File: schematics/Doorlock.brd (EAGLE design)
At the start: 65 x 56 mm, 40 parts, among them IC1 AT90S2313S, J1 RJ45, K1 G5V1, K2 G5V1, X1 RASPI_BOARD_B+#_H, X2 RIA182-04, X4 RIA182-05

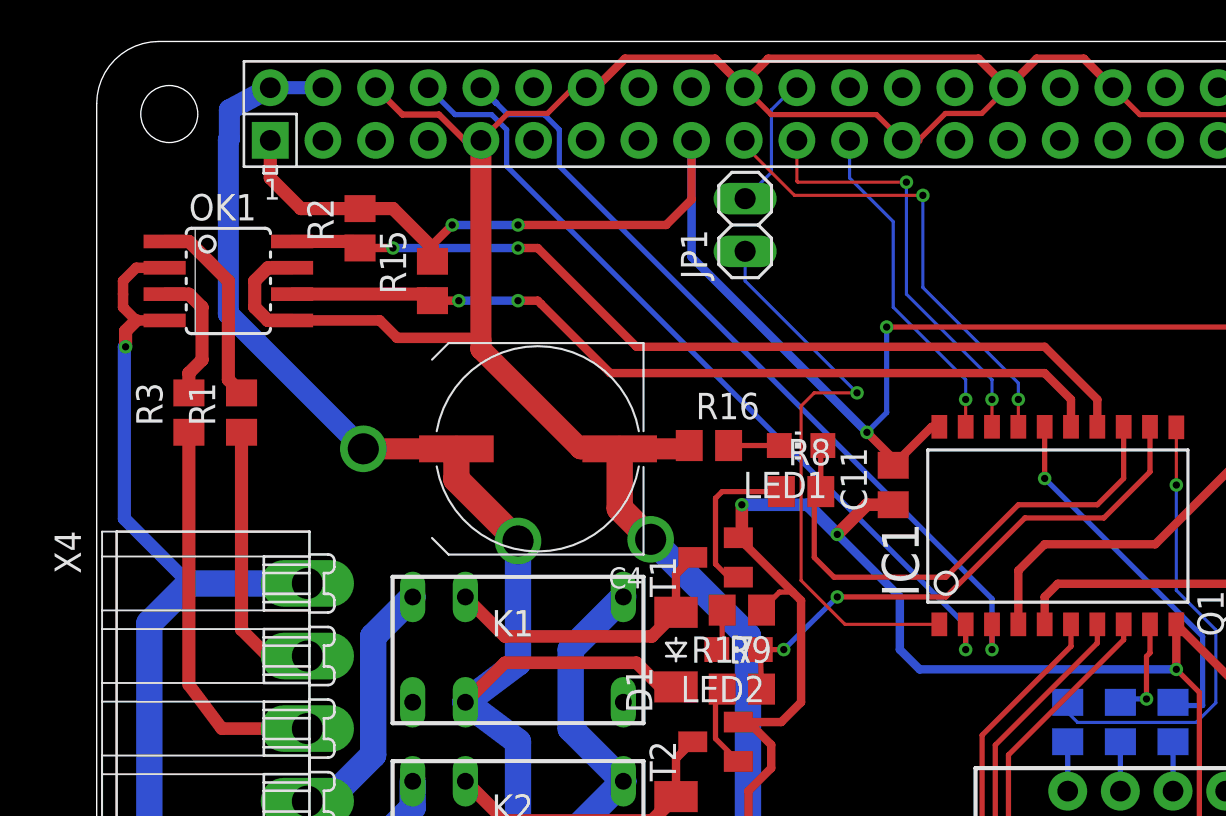
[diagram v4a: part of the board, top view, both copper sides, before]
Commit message: schematics: decouple optocoupler
Signed-off-by: Ralf Ramsauer <ralf@binary-kitchen.de>
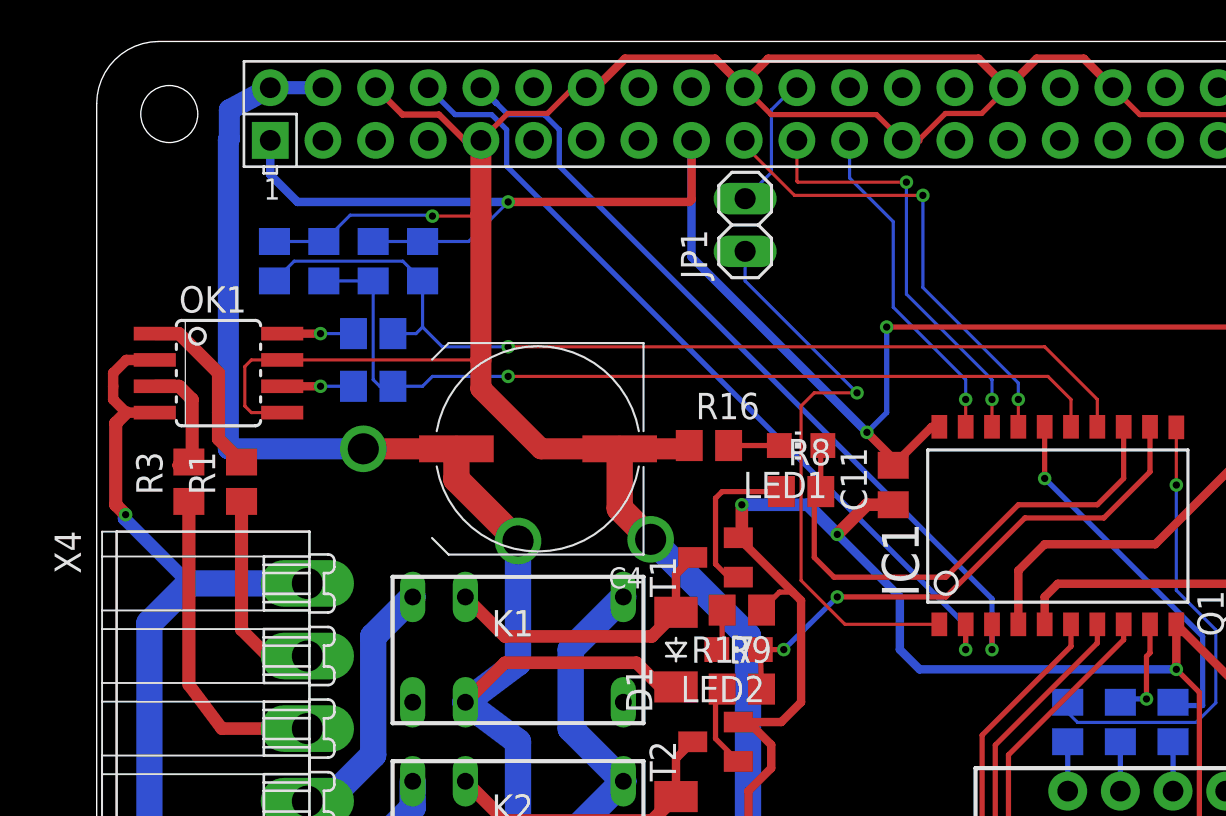
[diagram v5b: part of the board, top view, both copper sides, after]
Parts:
- added C5, C6: 100n, rcl:C0805
- added R18, R19: 1k, rcl:R0805
- R15, R2: value 1k -> 10k
- moved OK1 4.47 mm to (5.87, 40.0)
- moved R2 3.41 mm to (15.7, 45.4), flipped to the bottom
- moved R1 3.33 mm to (6.99, 34.8)
- moved R3 3.33 mm to (4.45, 34.8)
- moved R15 3.01 mm to (13.3, 45.4), flipped to the bottom
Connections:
- new net N$3: OK1.6, R18.1
- new net N$5: OK1.8, R19.1
- net EMERGENCY_UNLOCK: now also C6.1, R18.2; no longer OK1.6
- net GND: now also C5.2, C6.2
- net TUERSTATUS: now also C5.1, R19.2; no longer OK1.8
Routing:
- net GND: track 264.3 -> 276.4 mm, vias 5 -> 6
- net VCC: track 110.3 -> 115.0 mm, vias 4 -> 3
- net GND2: track 68.0 -> 63.7 mm
- net +5V: track 82.9 -> 86.7 mm
- net TUERSTATUS: track 43.3 -> 47.0 mm, vias 2 -> 1
- net N$5: track 0.00 -> 3.44 mm, vias 0 -> 1
- net N$3: track 0.00 -> 3.44 mm, vias 0 -> 1
- net N$13: track 18.9 -> 15.6 mm
- net N$10: track 13.2 -> 9.89 mm
- net EMERGENCY_UNLOCK: track 41.0 -> 42.9 mm, vias 2 -> 1
- net N$14: track 9.53 -> 8.61 mm

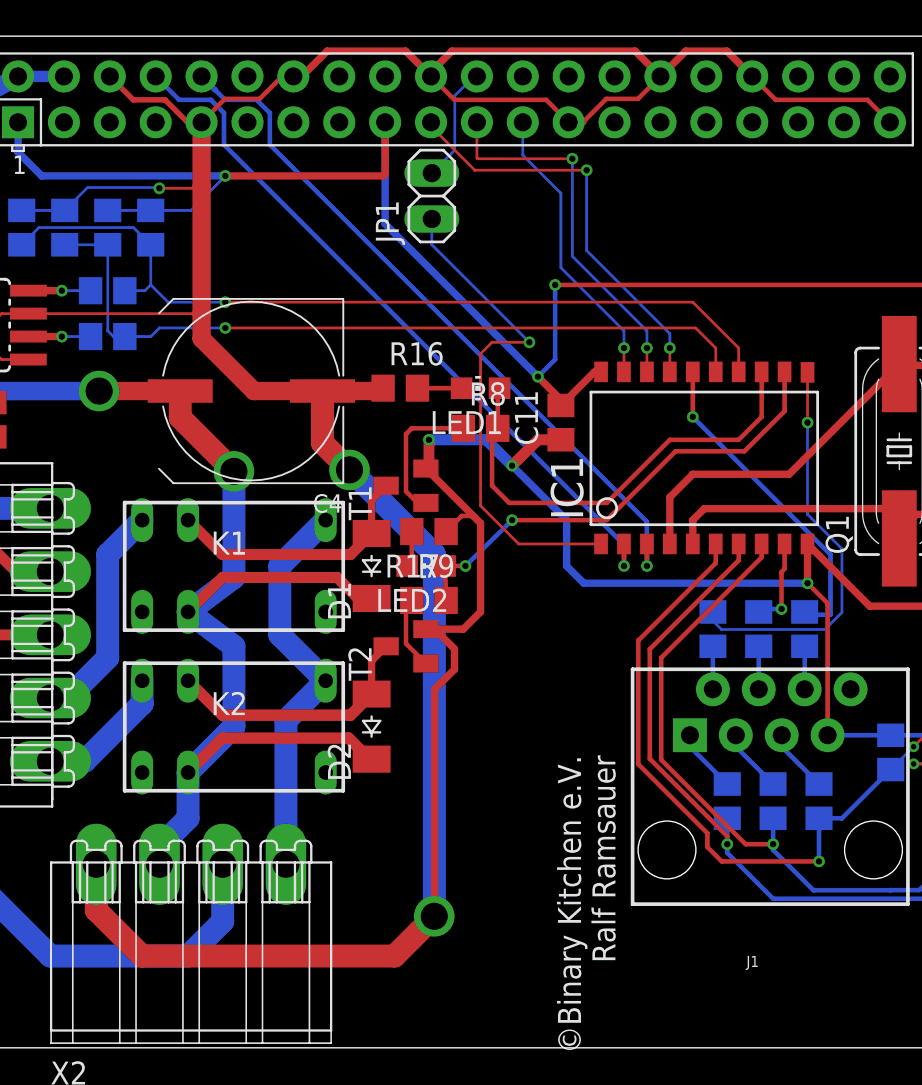
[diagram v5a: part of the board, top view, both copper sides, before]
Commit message: schematics: board: rearrange LEDs
Signed-off-by: Ralf Ramsauer <ralf@binary-kitchen.de>
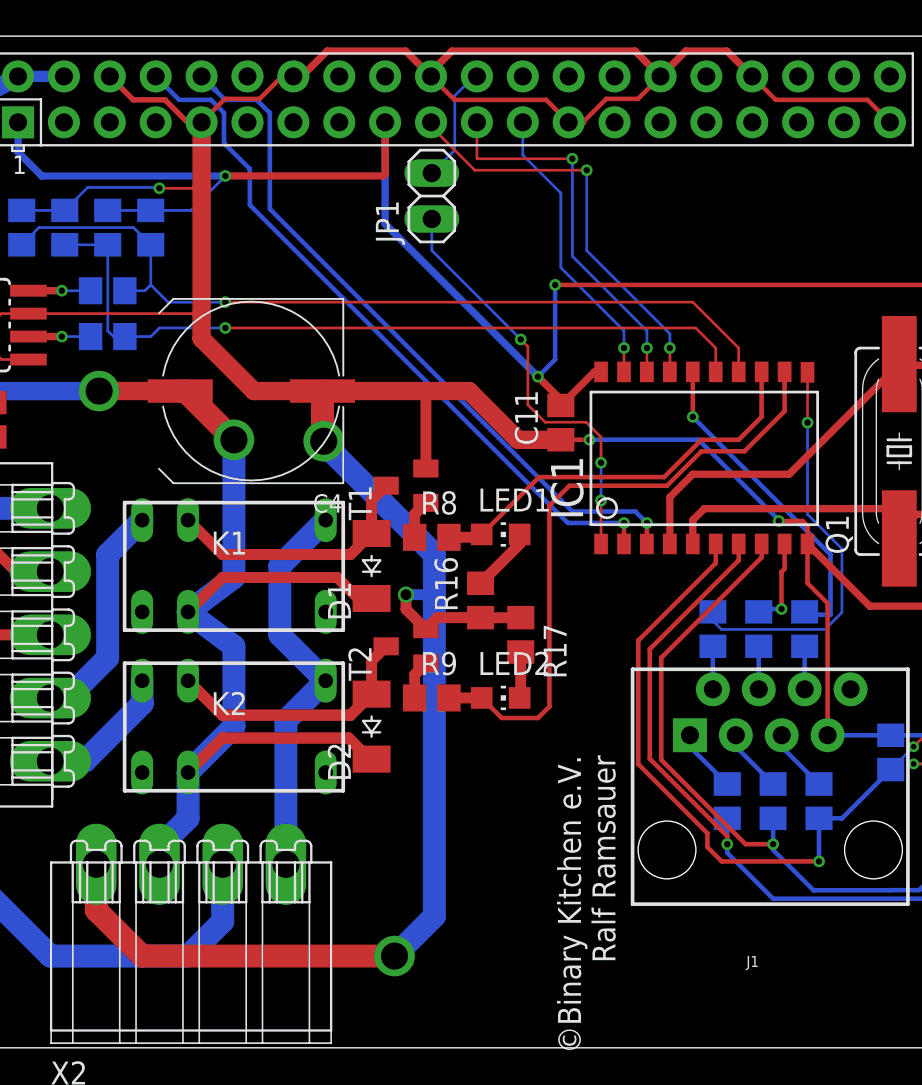
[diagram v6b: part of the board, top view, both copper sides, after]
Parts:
- moved R16 12.6 mm to (34.0, 24.8), turned to 90 degrees
- moved LED2 8.39 mm to (35.1, 19.4), turned to 270 degrees
- moved LED1 8.17 mm to (35.1, 28.4), turned to 270 degrees
- moved R17 7.65 mm to (36.2, 22.9), turned to 270 degrees
- moved R8 6.61 mm to (31.3, 28.3)
- moved R9 5.40 mm to (31.3, 19.4)
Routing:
- net GND: track 276.4 -> 255.2 mm
- net SCHNAPPER: track 26.4 -> 34.8 mm, vias 2 -> 0
- net N$27: track 7.85 -> 2.16 mm
- net N$1: track 28.0 -> 23.2 mm, vias 1 -> 3
- net BOLZEN: track 25.3 -> 22.8 mm
- net N$28: track 4.08 -> 2.16 mm
- net N$16: track 2.45 -> 3.60 mm
- net RXD: track 40.1 -> 39.5 mm
- net N$17: track 2.01 -> 2.57 mm

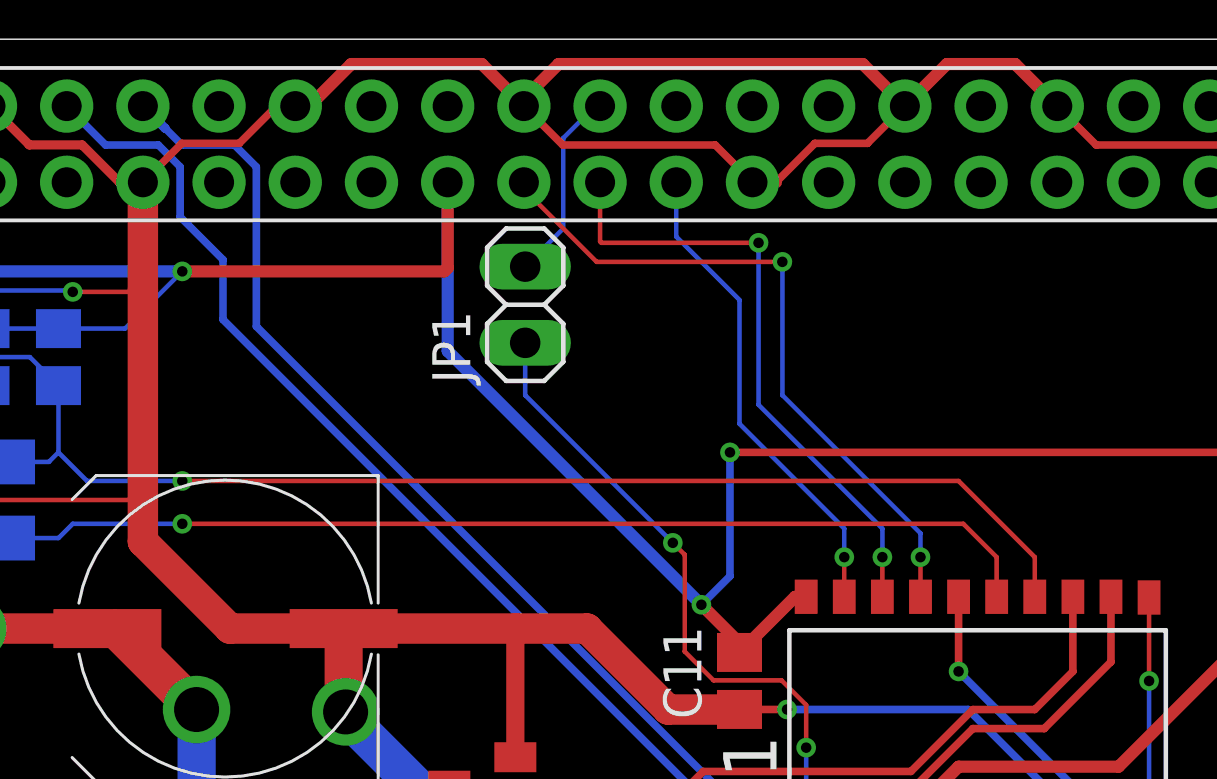
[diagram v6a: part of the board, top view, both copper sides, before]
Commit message: schematics: add door state jumper
Signed-off-by: Ralf Ramsauer <ralf@binary-kitchen.de>
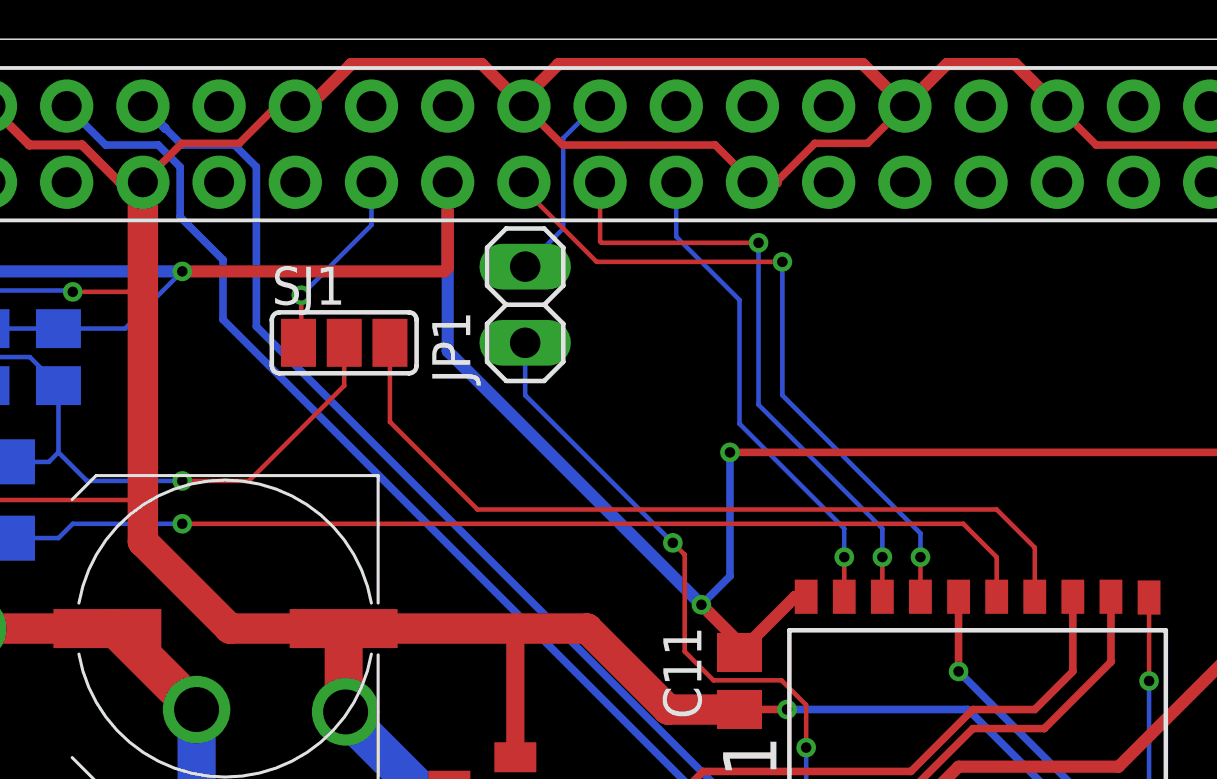
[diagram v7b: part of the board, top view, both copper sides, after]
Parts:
- added SJ1: (no value), jumper:SJ_2
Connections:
- new net TUERSTATUS_AVR: IC1.14, SJ1.3
- new net TUERSTATUS_PI: SJ1.1, X1.15
- net TUERSTATUS: now also SJ1.2; no longer IC1.14
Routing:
- net TUERSTATUS_AVR: track 0.00 -> 27.5 mm
- net TUERSTATUS: track 47.0 -> 24.4 mm
- net TUERSTATUS_PI: track 0.00 -> 6.36 mm, vias 0 -> 1
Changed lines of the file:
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@@
 <element name="R18" library="rcl" package="R0805" value="1k" x="13.335" y="39.37" rot="MR180"/>
 <element name="R19" library="rcl" package="R0805" value="1k" x="13.335" y="41.91" rot="MR180"/>
+<element name="SJ1" library="jumper" library_urn="urn:adsk.eagle:library:252" package="SJ_2" package3d_urn="urn:adsk.eagle:package:15474/1" value="" x="25.24125" y="45.87875"/>
 </elements>
 <signals>
@@
 <signal name="TUERSTATUS">
 <contactref element="R2" pad="1"/>
-<contactref element="IC1" pad="14"/>
 <via x="19.84375" y="41.275" extent="1-16" drill="0.35"/>
-<wire x1="45.72" y1="41.275" x2="48.26" y2="38.735" width="0.1524" layer="1"/>
-<wire x1="48.26" y1="38.735" x2="48.26" y2="37.4142" width="0.1524" layer="1"/>
-<wire x1="19.84375" y1="41.275" x2="45.72" y2="41.275" width="0.1524" layer="1"/>
 <contactref element="R19" pad="2"/>
 <contactref element="C5" pad="1"/>
@@
 <wire x1="15.71625" y1="42.2275" x2="16.66875" y2="41.275" width="0.1524" layer="16"/>
 <wire x1="16.66875" y1="41.275" x2="19.84375" y2="41.275" width="0.1524" layer="16"/>
+<contactref element="SJ1" pad="2"/>
+<wire x1="19.84375" y1="41.275" x2="22.06625" y2="41.275" width="0.1524" layer="1"/>
+<wire x1="22.06625" y1="41.275" x2="25.24125" y2="44.45" width="0.1524" layer="1"/>
+<wire x1="25.24125" y1="44.45" x2="25.24125" y2="45.87875" width="0.1524" layer="1"/>
 </signal>
 <signal name="N$10">
@@
 <wire x1="10.795" y1="41.91" x2="12.385" y2="41.91" width="0.1524" layer="16"/>
 </signal>
+<signal name="TUERSTATUS_AVR">
+<contactref element="SJ1" pad="3"/>
+<contactref element="IC1" pad="14"/>
+<wire x1="26.76525" y1="45.87875" x2="26.76525" y2="43.2435" width="0.1524" layer="1"/>
+<wire x1="26.76525" y1="43.2435" x2="29.68625" y2="40.3225" width="0.1524" layer="1"/>
+<wire x1="29.68625" y1="40.3225" x2="46.99" y2="40.3225" width="0.1524" layer="1"/>
+<wire x1="46.99" y1="40.3225" x2="48.26" y2="39.0525" width="0.1524" layer="1"/>
+<wire x1="48.26" y1="39.0525" x2="48.26" y2="37.4142" width="0.1524" layer="1"/>
+</signal>
+<signal name="TUERSTATUS_PI">
+<contactref element="SJ1" pad="1"/>
+<contactref element="X1" pad="15"/>
+<wire x1="23.71725" y1="45.87875" x2="23.8125" y2="45.974" width="0.1524" layer="1"/>
+<wire x1="23.8125" y1="45.974" x2="23.8125" y2="47.46625" width="0.1524" layer="1"/>
+<via x="23.8125" y="47.46625" extent="1-16" drill="0.35"/>
+<wire x1="23.8125" y1="47.46625" x2="26.15" y2="49.80375" width="0.1524" layer="16"/>
+<wire x1="26.15" y1="49.80375" x2="26.15" y2="51.23" width="0.1524" layer="16"/>
+</signal>
 </signals>

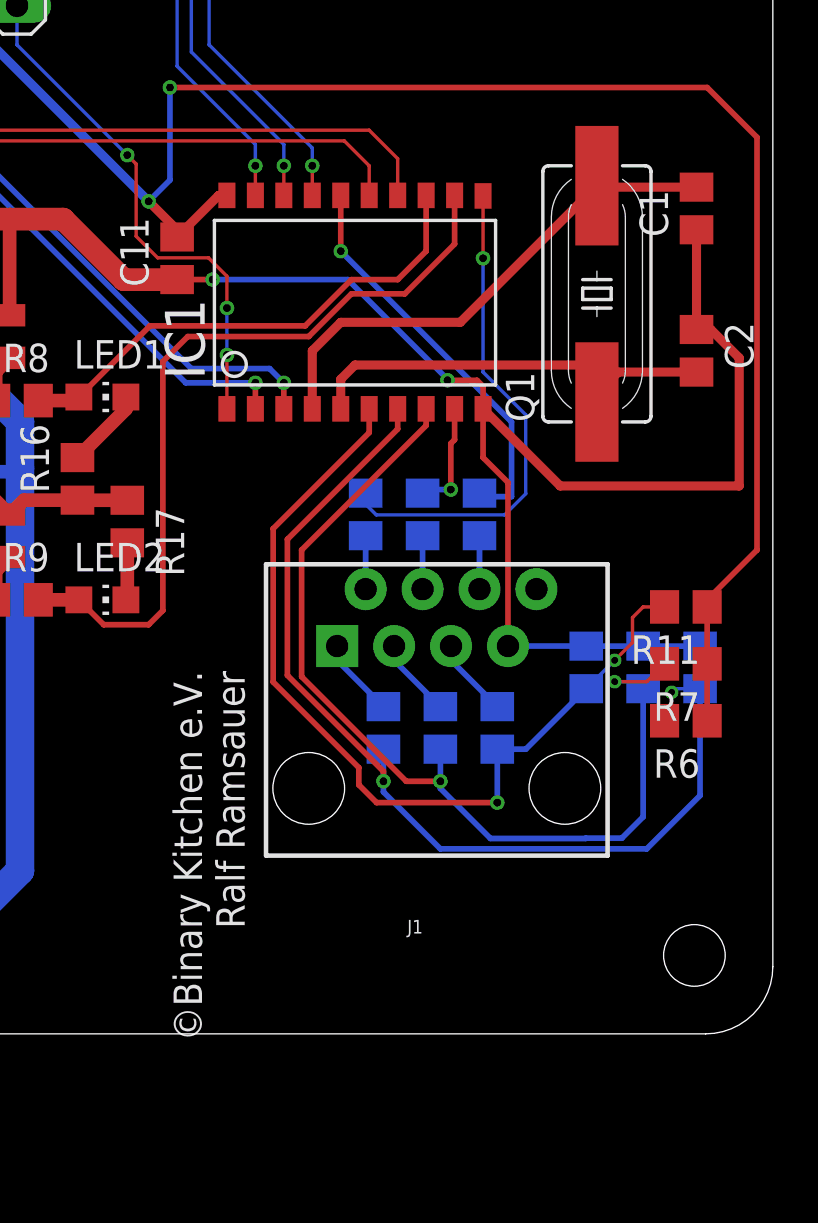
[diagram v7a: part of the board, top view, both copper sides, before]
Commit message: schematics: board: move RJ45 jack to the left
Signed-off-by: Ralf Ramsauer <ralf@binary-kitchen.de>
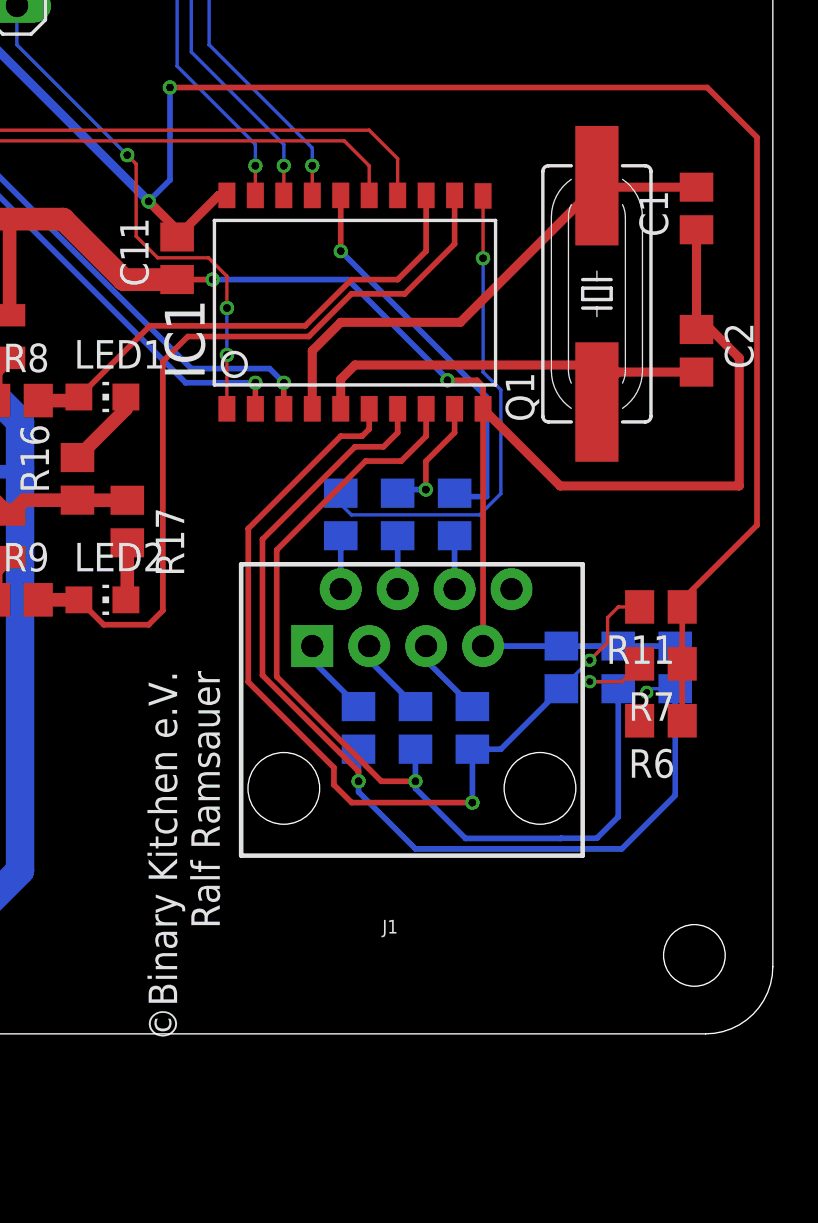
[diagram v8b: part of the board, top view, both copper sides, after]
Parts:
- moved R12 1.11 mm to (48.3, 23.2)
- moved R14 1.11 mm to (50.8, 23.2)
- moved C3 1.11 mm to (55.6, 16.4)
- moved C8 1.11 mm to (58.1, 16.4)
- moved C9 1.11 mm to (60.6, 16.4)
- moved J1 1.11 mm to (48.9, 11.0)
- moved R10 1.11 mm to (49.1, 13.7)
- moved R11 1.11 mm to (60.0, 19.1)
- moved R13 1.11 mm to (45.7, 23.2)
- moved R4 1.11 mm to (46.5, 13.7)
- moved R5 1.11 mm to (51.6, 13.7)
- moved R6 1.11 mm to (60.0, 14.0)
- moved R7 1.11 mm to (60.0, 16.5)
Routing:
- net BUTTON_GREEN: track 44.2 -> 45.6 mm
- net BUTTON_YELLOW: track 46.0 -> 47.2 mm
- net BUTTON_RED: track 39.8 -> 40.8 mm
